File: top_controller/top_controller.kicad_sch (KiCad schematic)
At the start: 50 parts, among them J1 SWD, SW1 RESET, U1 STM32F103C8Tx, Y1 8MHz

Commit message: schematic is finished (except LEDs)
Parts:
- added J2: USB_C_Receptacle_USB2.0, symbol Connector:USB_C_Receptacle_USB2.0
- added R3, R4: 5k1, symbol Device:R
- added U2: EPM78V2, symbol top_controller:EPM78V2
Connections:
- net AVDD: now also U2. (Vout)
- net AVSS: now also U2. (Vout)
- net GND: now also J2.A1 (GND), J2.A12 (GND), J2.B1 (GND), J2.B12 (GND), J2.S1 (SHIELD), R3.2, R4.1
- net PIN_VCC: now also U2.1 (Vin)
- net SWCLK: now also J2.B8 (SBU2)
- net SWDIO: now also J2.A8 (SBU1)
- net USB_VBUS: now reaches C?.1, U?.1 (IN), U?.2 (IN), U?.3 (IN), U?.4 (EN/UV)
- net USB_VBUS: now also J2.A4 (VBUS), J2.A9 (VBUS), J2.B4 (VBUS), J2.B9 (VBUS)
- new net: J2.B5 (CC2), R4.2
- new net: J2.A5 (CC1), R3.1
- new net USB_DM: J2.A7 (D-), J2.B7 (D-)
- new net USB_DP: J2.A6 (D+), J2.B6 (D+)
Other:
- title: (none) -> Photonic control curcuit
- moved on the sheet: C1, C2, C3, C4, C5, C6, C7, C8, C?, J1, J?, R1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

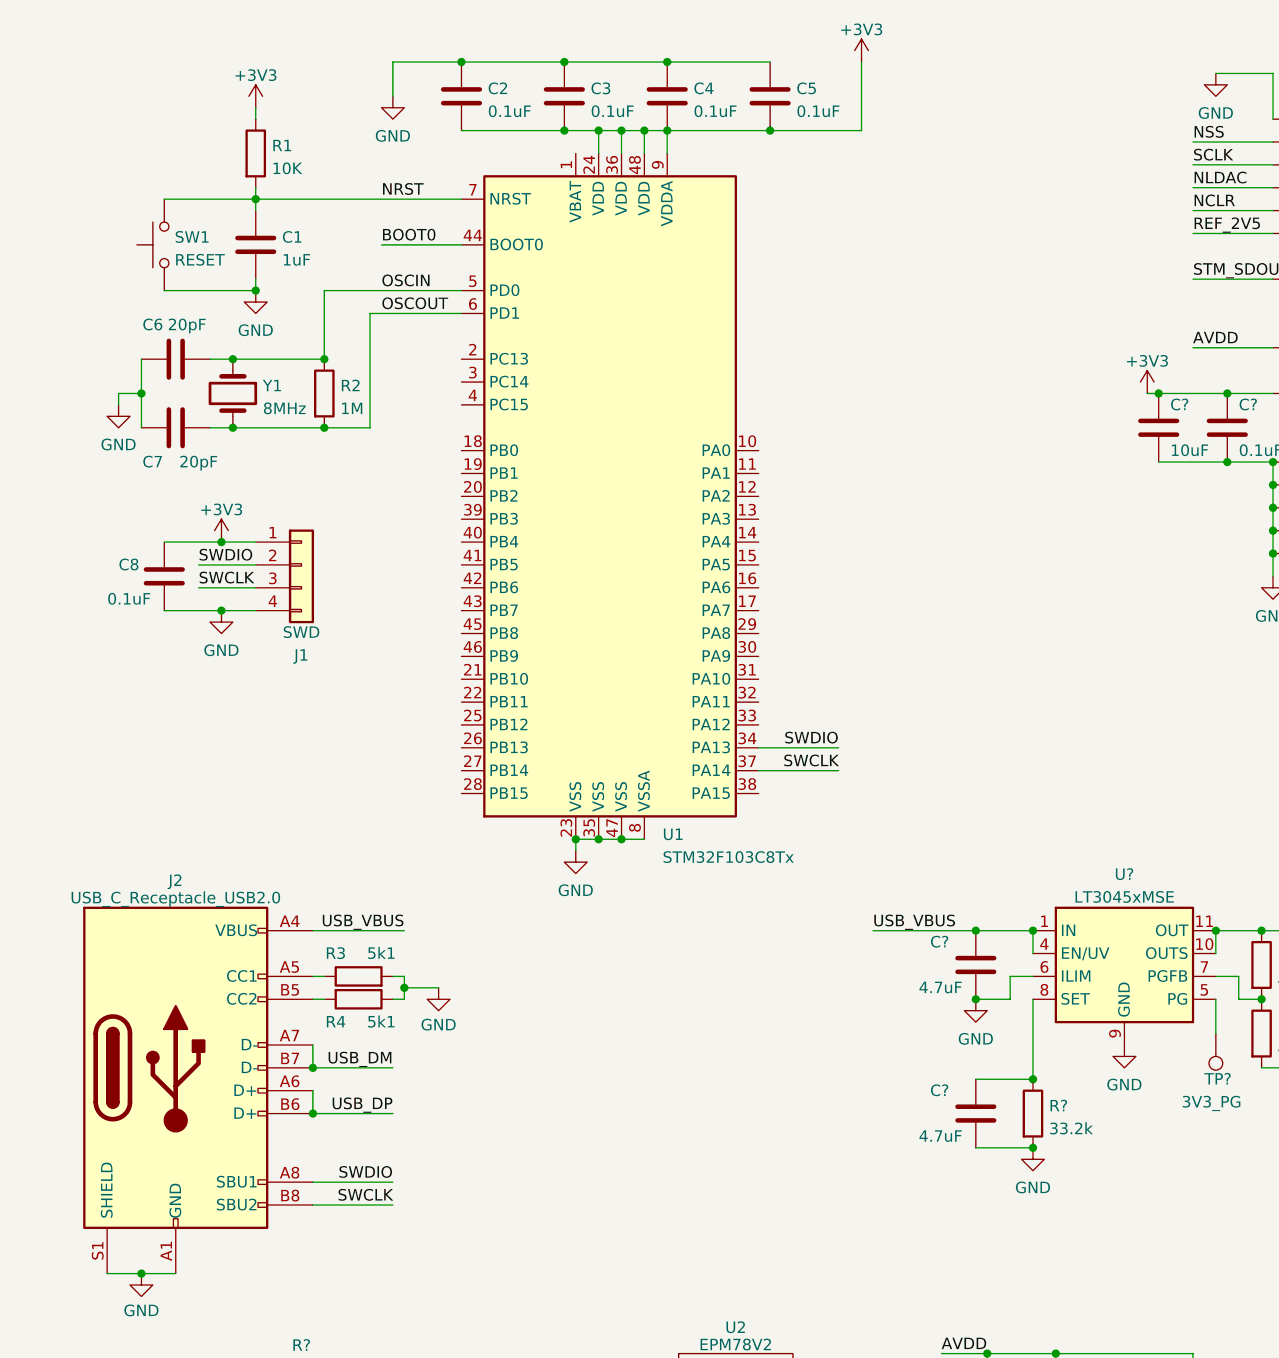
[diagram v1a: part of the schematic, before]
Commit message: Finalized the schematic Added LEDs and UART
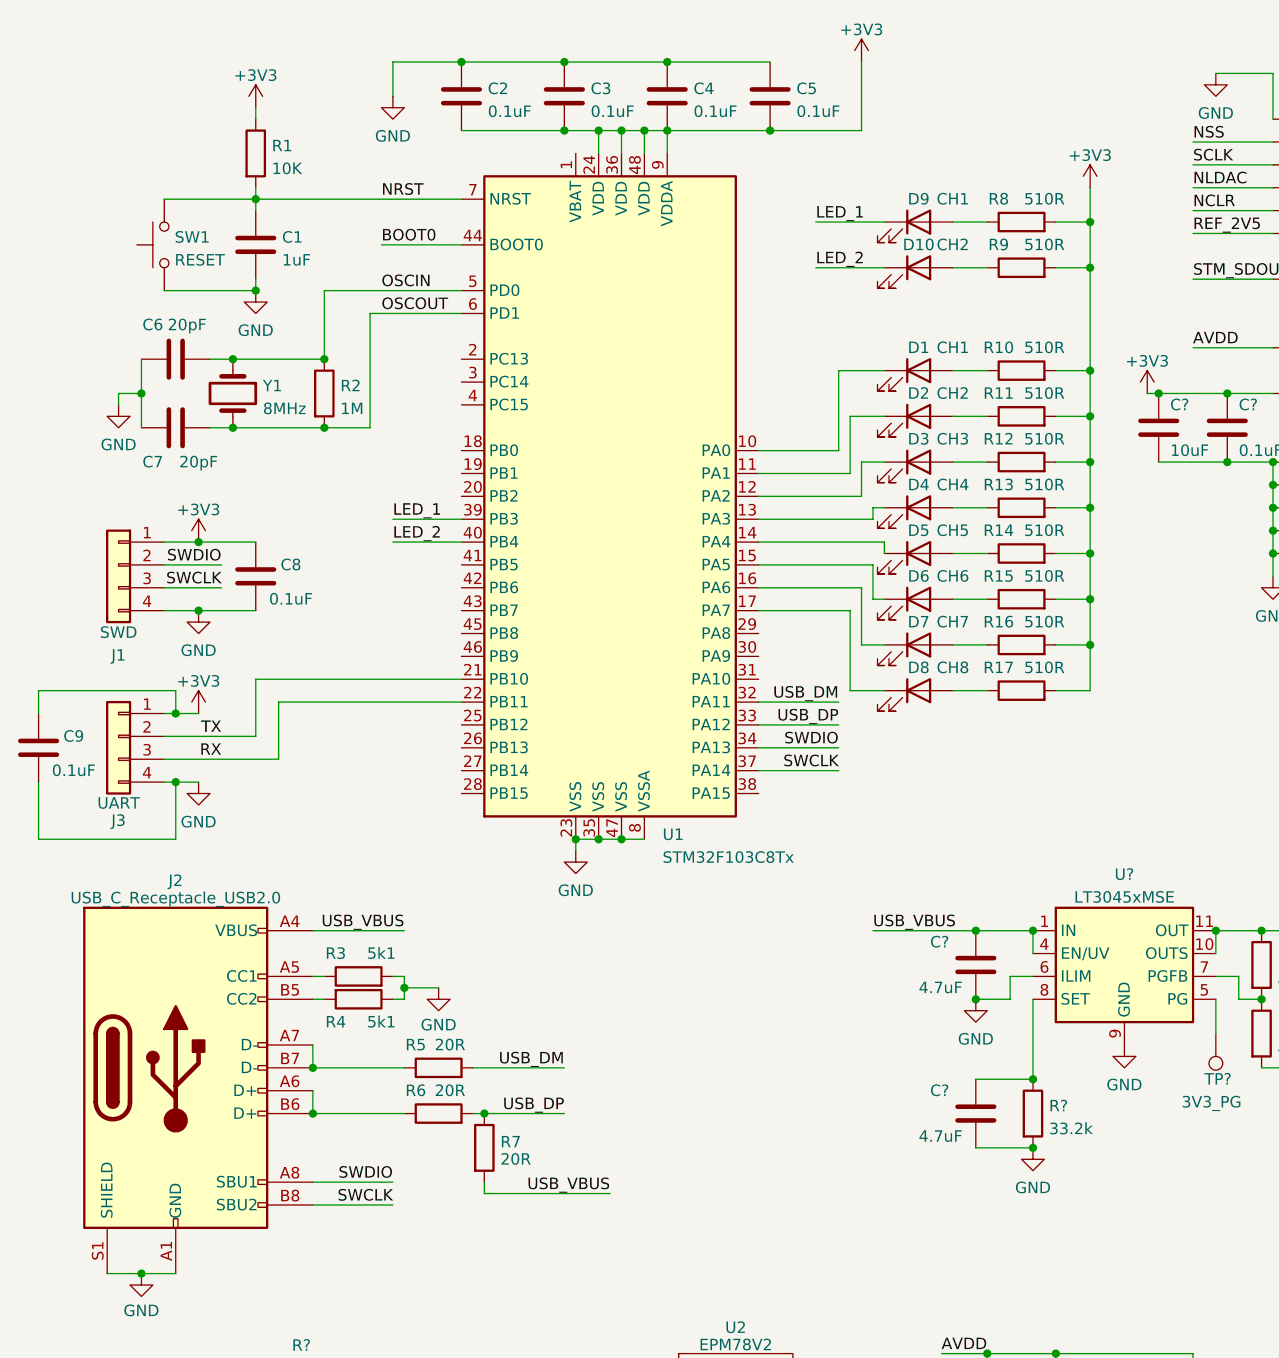
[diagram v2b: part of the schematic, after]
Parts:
- added C9: 0.1uF, symbol Device:C
- added D1, D9: CH1, symbol Device:LED
- added D10, D2: CH2, symbol Device:LED
- added D3: CH3, symbol Device:LED
- added D4: CH4, symbol Device:LED
- added D5: CH5, symbol Device:LED
- added D6: CH6, symbol Device:LED
- added D7: CH7, symbol Device:LED
- added D8: CH8, symbol Device:LED
- added J3: UART, symbol Connector_Generic:Conn_01x04
- added R10, R11, R12, R13, R14, R15, R16, R17, R8, R9: 510R, symbol Device:R
- added R5, R6, R7: 20R, symbol Device:R
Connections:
- net +3V3: now also C9.1, J3.1 (Pin_1), R10.2, R11.2, R12.2, R13.2, R14.2, R15.2, R16.2, R17.2, R8.2, R9.2
- net GND: now also C9.2, J3.4 (Pin_4)
- net USB_DM: now also U1.32 (PA11), R5.2; no longer J2.A7 (D-), J2.B7 (D-)
- net USB_DP: now also U1.33 (PA12), R6.2, R7.1; no longer J2.A6 (D+), J2.B6 (D+)
- net USB_VBUS: now also R7.2
- net at U1.10 (PA0): now also D1.1 (K)
- net at U1.11 (PA1): now also D2.1 (K)
- net at U1.12 (PA2): now also D3.1 (K)
- net at U1.13 (PA3): now also D4.1 (K)
- net at U1.14 (PA4): now also D5.1 (K)
- net at U1.15 (PA5): now also D6.1 (K)
- net at U1.16 (PA6): now also D7.1 (K)
- net at U1.17 (PA7): now also D8.1 (K)
- net TX: now reaches U1.21 (PB10)
- net TX: now also J3.2 (Pin_2)
- net RX: now reaches U1.22 (PB11)
- net RX: now also J3.3 (Pin_3)
- net LED_1: now reaches U1.39 (PB3)
- net LED_1: now also D9.1 (K)
- net LED_2: now reaches U1.40 (PB4)
- net LED_2: now also D10.1 (K)
- new net: D4.2 (A), R13.1
- new net: D5.2 (A), R14.1
- new net: D10.2 (A), R9.1
- new net: D3.2 (A), R12.1
- new net: J2.A7 (D-), J2.B7 (D-), R5.1
- new net: D9.2 (A), R8.1
- new net: D7.2 (A), R16.1
- new net: J2.A6 (D+), J2.B6 (D+), R6.1
- new net: D6.2 (A), R15.1
- new net: D2.2 (A), R11.1
- new net: D1.2 (A), R10.1
- new net: D8.2 (A), R17.1
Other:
- moved on the sheet: C8, J1

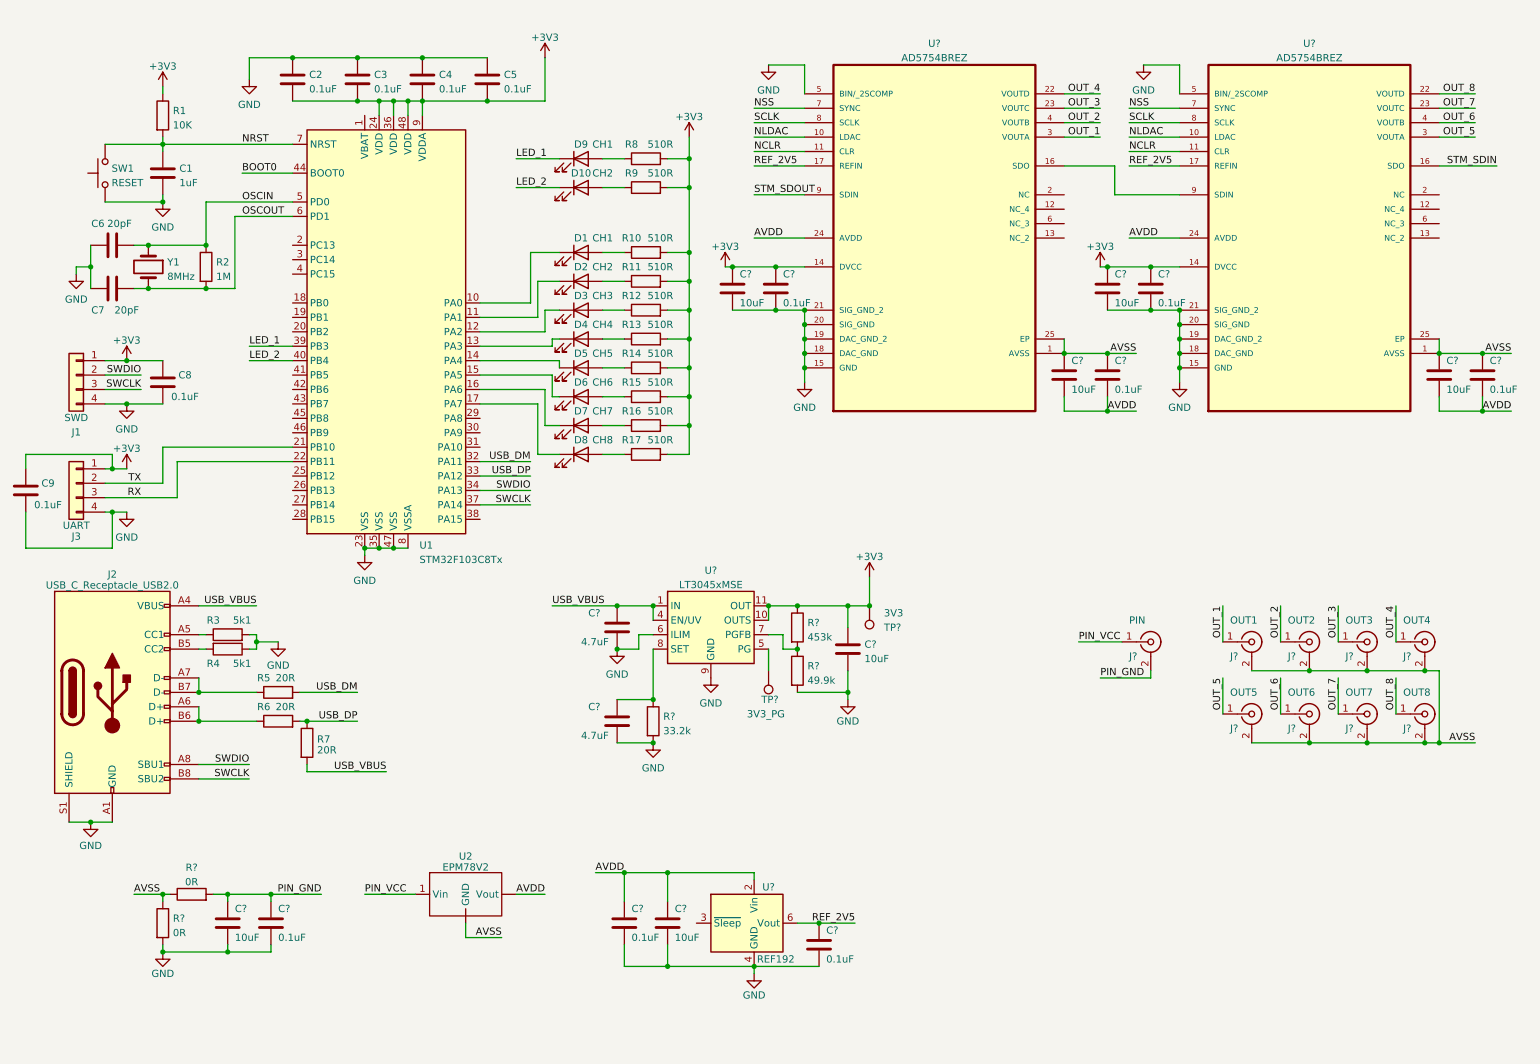
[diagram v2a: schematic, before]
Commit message: Small fixes - Power supplied to VBAT of STM32 - Added 10uF cap for the whole STM32 - Added BOOT0 switch - Labelled some unlabelled nets - Added resistor between USB connector SHIELD and GND - Marked all unused pins - Added posibility of pulling USB_DP to 3v3 instead of USB_VBUS - Added LED indication for power lines - Rearranged the schematic - Reannotated - Fixed couple missing connections and annotated power (for DRC)
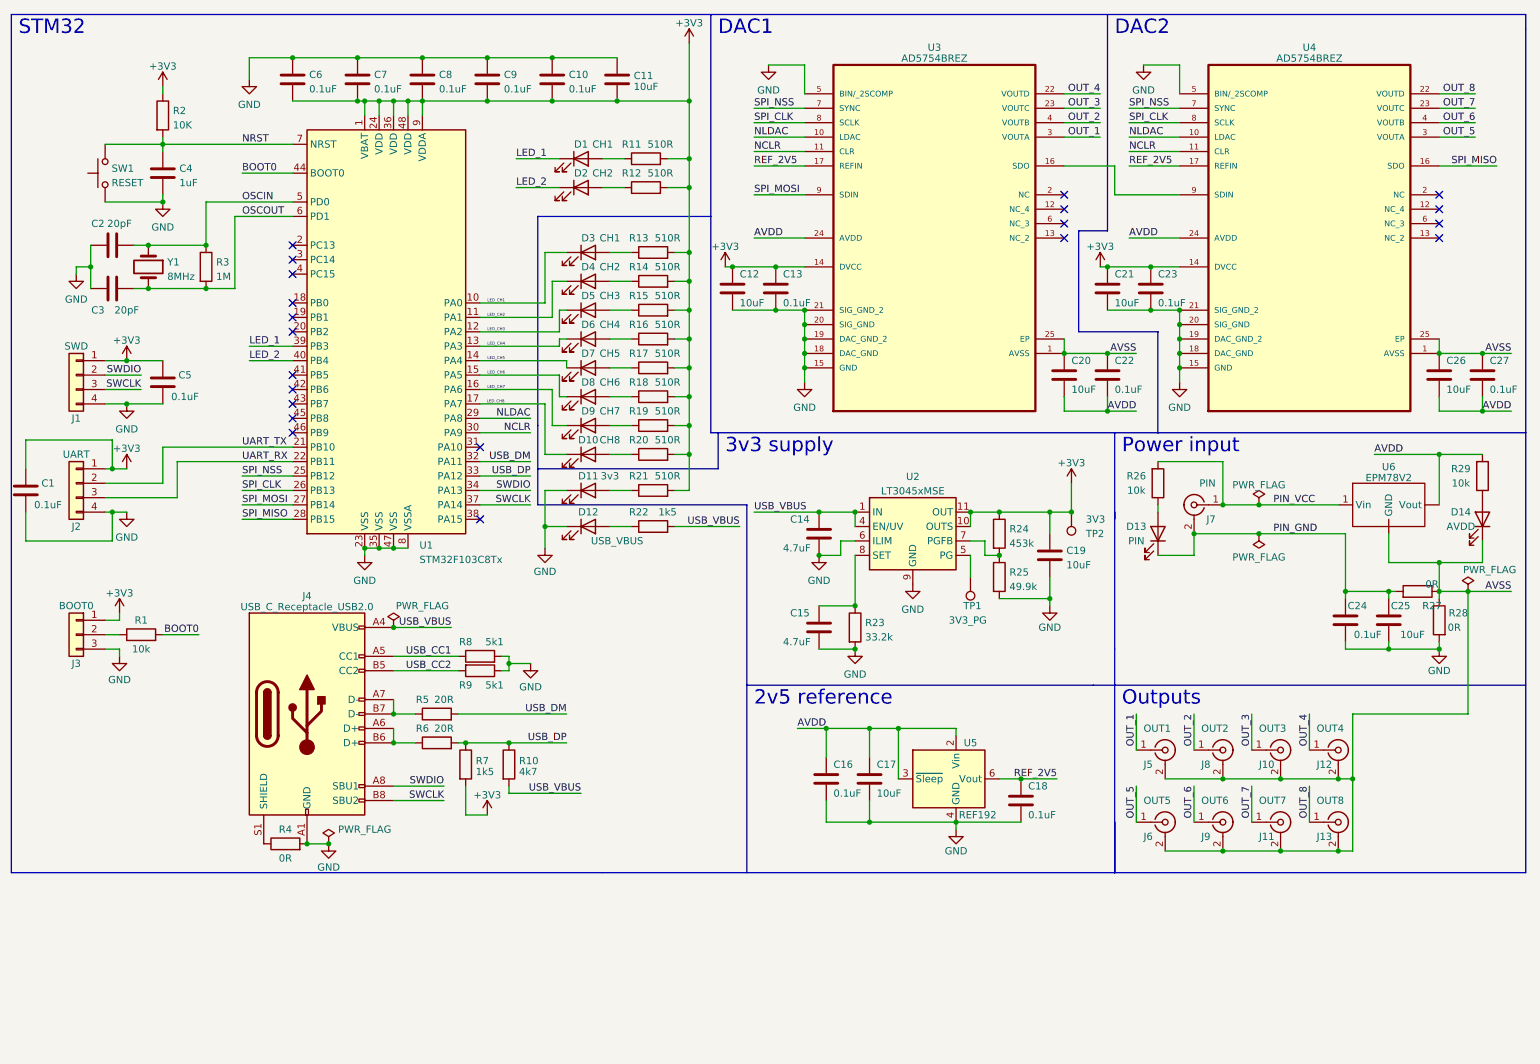
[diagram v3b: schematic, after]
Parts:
- added C10: 0.1uF, symbol Device:C
- added C11: 10uF, symbol Device:C
- added D11: 3v3, symbol Device:LED
- added D12: USB_VBUS, symbol Device:LED
- added D13: PIN, symbol Device:LED
- added D14: AVDD, symbol Device:LED
- added J3: BOOT0, symbol Connector_Generic:Conn_01x03
- added R1, R26, R29: 10k, symbol Device:R
- added R21: 510R, symbol Device:R
- added R22, R7: 1k5, symbol Device:R
- added R4: 0R, symbol Device:R
- R10: renamed from R7; value 20R -> 4k7
- gave numbers to parts that had none: 36
- renumbered C9 to C1, C6 to C2, C7 to C3, C1 to C4, C8 to C5, C2 to C6, C3 to C7, C4 to C8, C5 to C9, D9 to D1, D8 to D10, D10 to D2, D1 to D3, D2 to D4, D3 to D5, D4 to D6, D5 to D7, D6 to D8, D7 to D9, J3 to J2, J2 to J4, R8 to R11, R9 to R12, R10 to R13, R11 to R14, R12 to R15, R13 to R16, R14 to R17, R15 to R18, R16 to R19, R1 to R2, R17 to R20, R2 to R3, R3 to R8, R4 to R9, U2 to U6
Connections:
- net NSS is gone; now on net SPI_NSS: U3.7 (SYNC), U4.7 (SYNC)
- net SCLK is gone; now on net SPI_CLK: U3.8 (SCLK), U4.8 (SCLK)
- net STM_SDIN is gone; now on net SPI_MISO: U4.16 (SDO)
- net STM_SDOUT is gone; now on net SPI_MOSI: U3.9 (SDIN)
- net +3V3: now also U1.1 (VBAT), C10.2, C11.2, J3.1 (Pin_1), R21.2, R7.2
- net AVDD: now also U5.3 (~{Sleep}), R29.2
- net AVSS: now also D14.1 (K)
- net BOOT0: now also R1.2
- net GND: now also C10.1, C11.1, D11.1 (K), D12.1 (K), J3.3 (Pin_3), R4.2; no longer J4.S1 (SHIELD)
- net NCLR: now also U1.30 (PA9)
- net NLDAC: now also U1.29 (PA8)
- net PIN_GND: now also D13.1 (K)
- net PIN_VCC: now also R26.2
- net USB_DP: now also R7.1
- net USB_VBUS: now also R22.2
- net LED_CH4: now reaches D6.1 (K), U1.13 (PA3)
- net LED_CH3: now reaches D5.1 (K), U1.12 (PA2)
- net LED_CH5: now reaches D7.1 (K), U1.14 (PA4)
- net LED_CH6: now reaches D8.1 (K), U1.15 (PA5)
- net USB_CC2: now reaches J4.B5 (CC2), R9.2
- net LED_CH1: now reaches D3.1 (K), U1.10 (PA0)
- net LED_CH8: now reaches D10.1 (K), U1.17 (PA7)
- net LED_CH7: now reaches D9.1 (K), U1.16 (PA6)
- net USB_CC1: now reaches J4.A5 (CC1), R8.1
- net LED_CH2: now reaches D4.1 (K), U1.11 (PA1)
- net SPI_NSS: now reaches U1.25 (PB12)
- net SPI_CLK: now reaches U1.26 (PB13)
- net SPI_MOSI: now reaches U1.27 (PB14)
- net SPI_MISO: now reaches U1.28 (PB15)
- net RX renamed UART_RX
- net TX renamed UART_TX
- new net: D11.2 (A), R21.1
- new net: J4.S1 (SHIELD), R4.1
- new net: D12.2 (A), R22.1
- new net: J3.2 (Pin_2), R1.1
- new net: D13.2 (A), R26.1
- new net: D14.2 (A), R29.1
- no-connect marks 0 -> 21
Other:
- note added: "2v5 reference"
- note added: "3v3 supply"
- note added: "DAC1"
- note added: "DAC2"
- note added: "Outputs"
- note added: "Power input"
- note added: "STM32"
- moved on the sheet: C14, C15, C16, C17, C18, C19, C24, C25, D10, D3, D4, D5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
